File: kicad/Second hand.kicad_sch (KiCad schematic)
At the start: 66 parts, among them U001 74HC595, U002 74HC595

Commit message: First completely routed version
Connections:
- net Px0 renamed Sx0
- net Px1 renamed Sx1
- net Px2 renamed Sx2
- net Px3 renamed Sx3
- net Px4 renamed Sx4
- net Px5 renamed Sx5
- net Px6 renamed Sx6
- net Px7 renamed Sx7
- net Px8 renamed Sx8
- net Px9 renamed Sx9
- net Q0x renamed S0x
- net Q1x renamed S1x
- net Q2x renamed S2x
- net Q3x renamed S3x
- net Q4x renamed S4x
- net Q5x renamed S5x

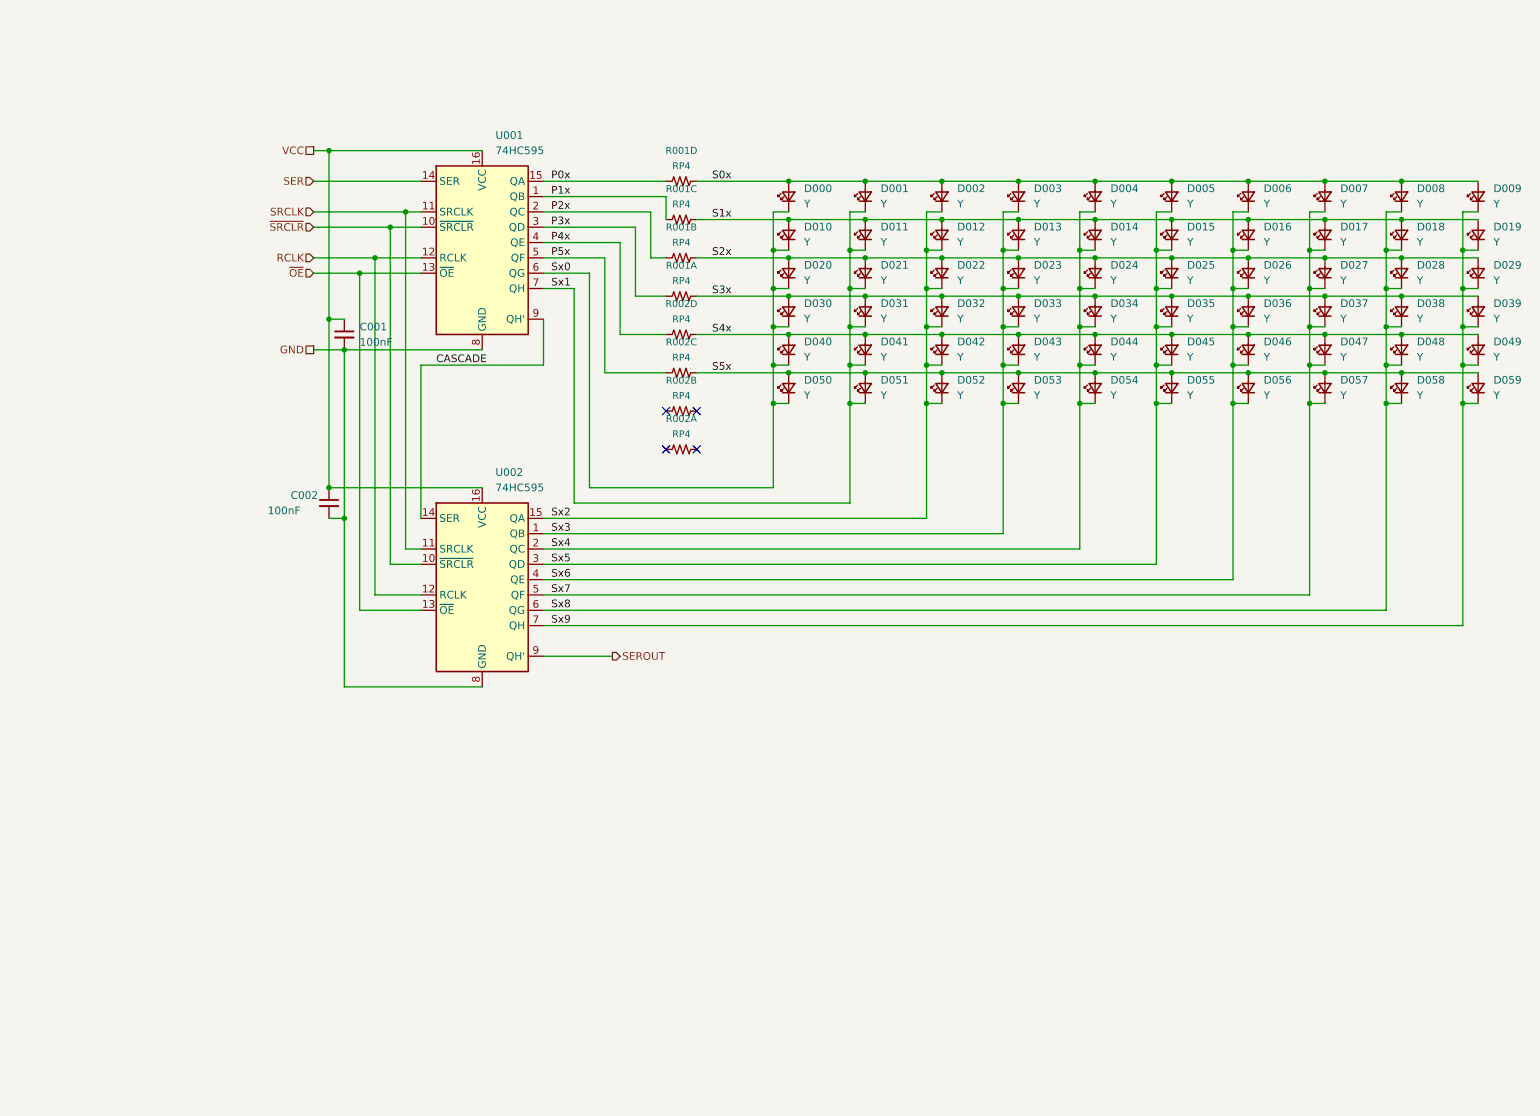
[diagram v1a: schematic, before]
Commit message: Add notes for diode voltages
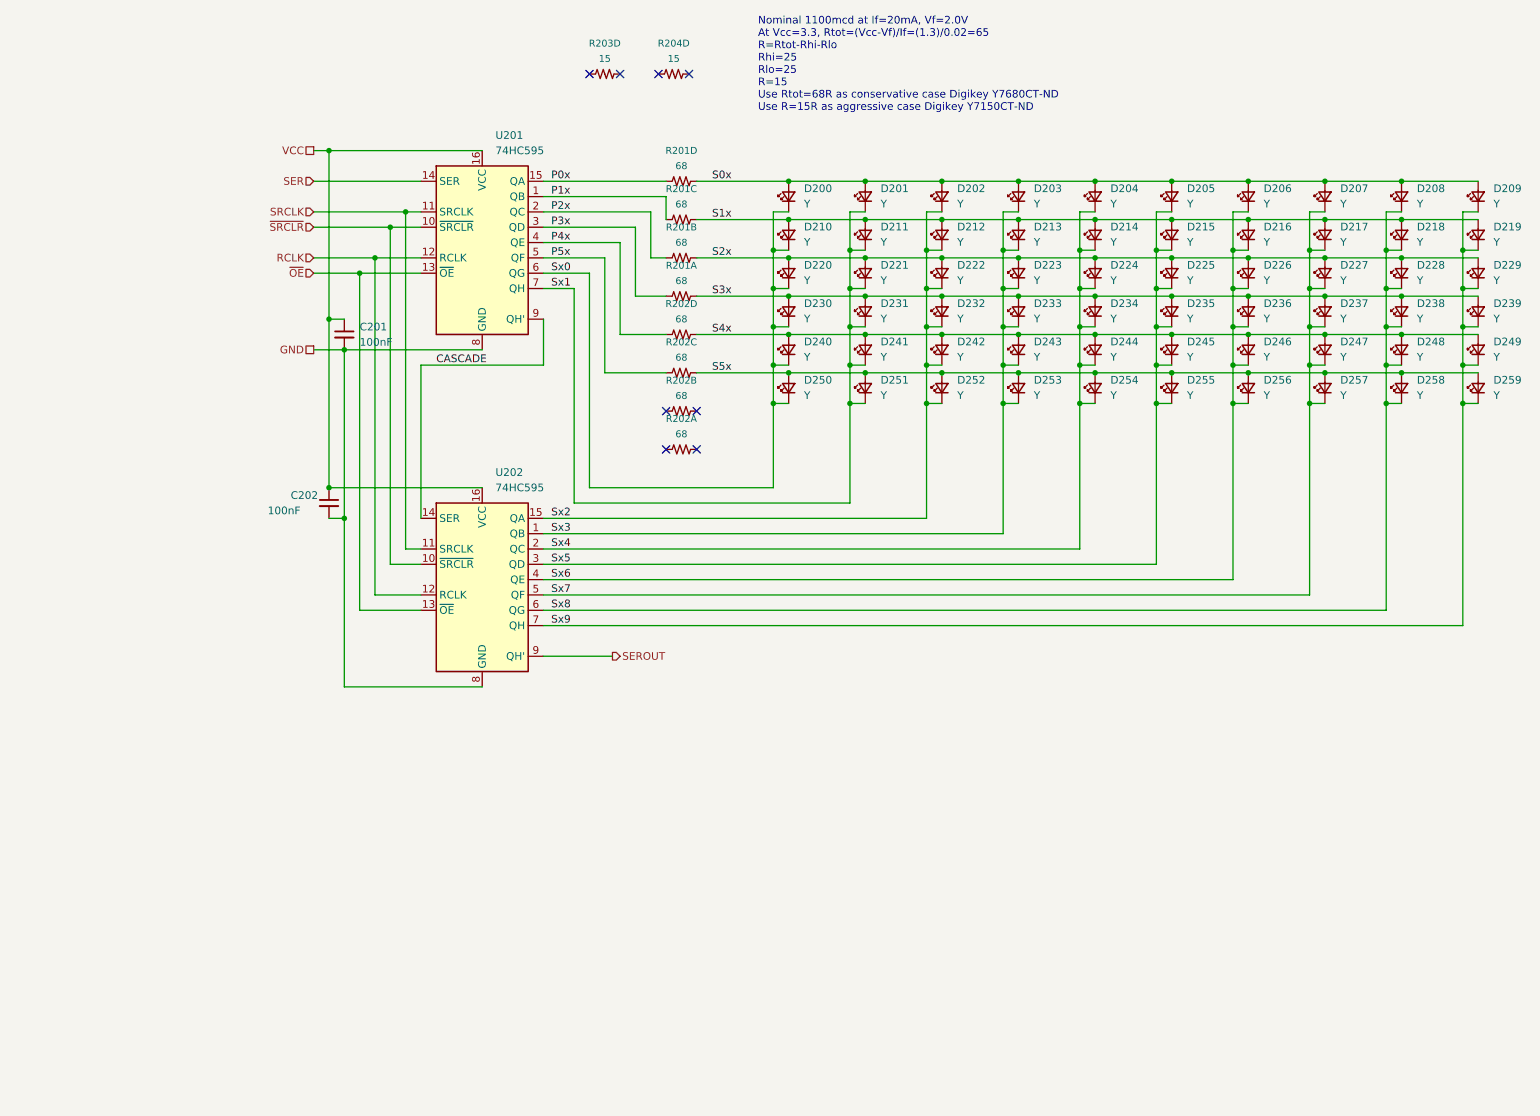
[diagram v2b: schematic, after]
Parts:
- added R203, R204: 15, KwanSystems:R_Array_Convex_4x0402, symbol KwanSystems:RP4
- C201: renamed from C001; Digikey (none) -> 445-5613-1-ND; Part Number (none) -> CGA2B1X7R1C104K050BC; Purpose (none) -> Second hand decoder bypass
- C202: renamed from C002; Digikey (none) -> 445-5613-1-ND; Part Number (none) -> CGA2B1X7R1C104K050BC; Purpose (none) -> Second hand decoder bypass
- D200: renamed from D000; Purpose (none) -> Yellow second hand
- D201: renamed from D001; Purpose (none) -> Yellow second hand
- D202: renamed from D002; Purpose (none) -> Yellow second hand
- D203: renamed from D003; Purpose (none) -> Yellow second hand
- D204: renamed from D004; Purpose (none) -> Yellow second hand
- D205: renamed from D005; Purpose (none) -> Yellow second hand
- D206: renamed from D006; Purpose (none) -> Yellow second hand
- D207: renamed from D007; Purpose (none) -> Yellow second hand
- D208: renamed from D008; Purpose (none) -> Yellow second hand
- D209: renamed from D009; Purpose (none) -> Yellow second hand
- D210: renamed from D010; Purpose (none) -> Yellow second hand
- D211: renamed from D011; Purpose (none) -> Yellow second hand
- D212: renamed from D012; Purpose (none) -> Yellow second hand
- D213: renamed from D013; Purpose (none) -> Yellow second hand
- D214: renamed from D014; Purpose (none) -> Yellow second hand
- D215: renamed from D015; Purpose (none) -> Yellow second hand
- D216: renamed from D016; Purpose (none) -> Yellow second hand
- D217: renamed from D017; Purpose (none) -> Yellow second hand
- D218: renamed from D018; Purpose (none) -> Yellow second hand
- D219: renamed from D019; Purpose (none) -> Yellow second hand
- D220: renamed from D020; Purpose (none) -> Yellow second hand
- D221: renamed from D021; Purpose (none) -> Yellow second hand
- D222: renamed from D022; Purpose (none) -> Yellow second hand
- D223: renamed from D023; Purpose (none) -> Yellow second hand
- D224: renamed from D024; Purpose (none) -> Yellow second hand
- D225: renamed from D025; Purpose (none) -> Yellow second hand
- D226: renamed from D026; Purpose (none) -> Yellow second hand
- D227: renamed from D027; Purpose (none) -> Yellow second hand
- D228: renamed from D028; Purpose (none) -> Yellow second hand
- D229: renamed from D029; Purpose (none) -> Yellow second hand
- D230: renamed from D030; Purpose (none) -> Yellow second hand
- D231: renamed from D031; Purpose (none) -> Yellow second hand
- D232: renamed from D032; Purpose (none) -> Yellow second hand
- D233: renamed from D033; Purpose (none) -> Yellow second hand
- D234: renamed from D034; Purpose (none) -> Yellow second hand
- D235: renamed from D035; Purpose (none) -> Yellow second hand
- D236: renamed from D036; Purpose (none) -> Yellow second hand
- D237: renamed from D037; Purpose (none) -> Yellow second hand
- D238: renamed from D038; Purpose (none) -> Yellow second hand
- D239: renamed from D039; Purpose (none) -> Yellow second hand
- D240: renamed from D040; Purpose (none) -> Yellow second hand
- D241: renamed from D041; Purpose (none) -> Yellow second hand
- D242: renamed from D042; Purpose (none) -> Yellow second hand
- D243: renamed from D043; Purpose (none) -> Yellow second hand
- D244: renamed from D044; Purpose (none) -> Yellow second hand
- D245: renamed from D045; Purpose (none) -> Yellow second hand
- D246: renamed from D046; Purpose (none) -> Yellow second hand
- D247: renamed from D047; Purpose (none) -> Yellow second hand
- D248: renamed from D048; Purpose (none) -> Yellow second hand
- D249: renamed from D049; Purpose (none) -> Yellow second hand
- D250: renamed from D050; Purpose (none) -> Yellow second hand
- D251: renamed from D051; Purpose (none) -> Yellow second hand
- D252: renamed from D052; Purpose (none) -> Yellow second hand
- D253: renamed from D053; Purpose (none) -> Yellow second hand
- D254: renamed from D054; Purpose (none) -> Yellow second hand
- D255: renamed from D055; Purpose (none) -> Yellow second hand
- D256: renamed from D056; Purpose (none) -> Yellow second hand
- D257: renamed from D057; Purpose (none) -> Yellow second hand
- D258: renamed from D058; Purpose (none) -> Yellow second hand
- D259: renamed from D059; Purpose (none) -> Yellow second hand
- R201: renamed from R001; value RP4 -> 68; Digikey (none) -> Y7680CT-ND; Part Number (none) -> EXB-28V680JX; Purpose (none) -> Second hand conservative current limit
- R202: renamed from R002; value RP4 -> 68; Digikey (none) -> Y7680CT-ND; Part Number (none) -> EXB-28V680JX; Purpose (none) -> Second hand conservative current limit
- U201: renamed from U001; Part Number (none) -> 74HC595PW,118; Purpose (none) -> Hand Decoder
- U202: renamed from U002; Part Number (none) -> 74HC595PW,118; Purpose (none) -> Hand Decoder
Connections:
- no-connect marks 4 -> 8
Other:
- note added: "Nominal 1100mcd at If=20mA, Vf=2.0V At Vcc=3.3, Rtot=(Vcc-Vf)/If=(1.3)/0.02=65 R=Rtot-Rhi-Rlo Rhi=25 Rlo=25 R=15 Use Rtot=68R as conservative case Digikey Y7680CT-ND Use R=15R as aggressive case Digikey Y7150CT-ND"

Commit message: Put MOSFET switch transistors in place. We won't end up using these.
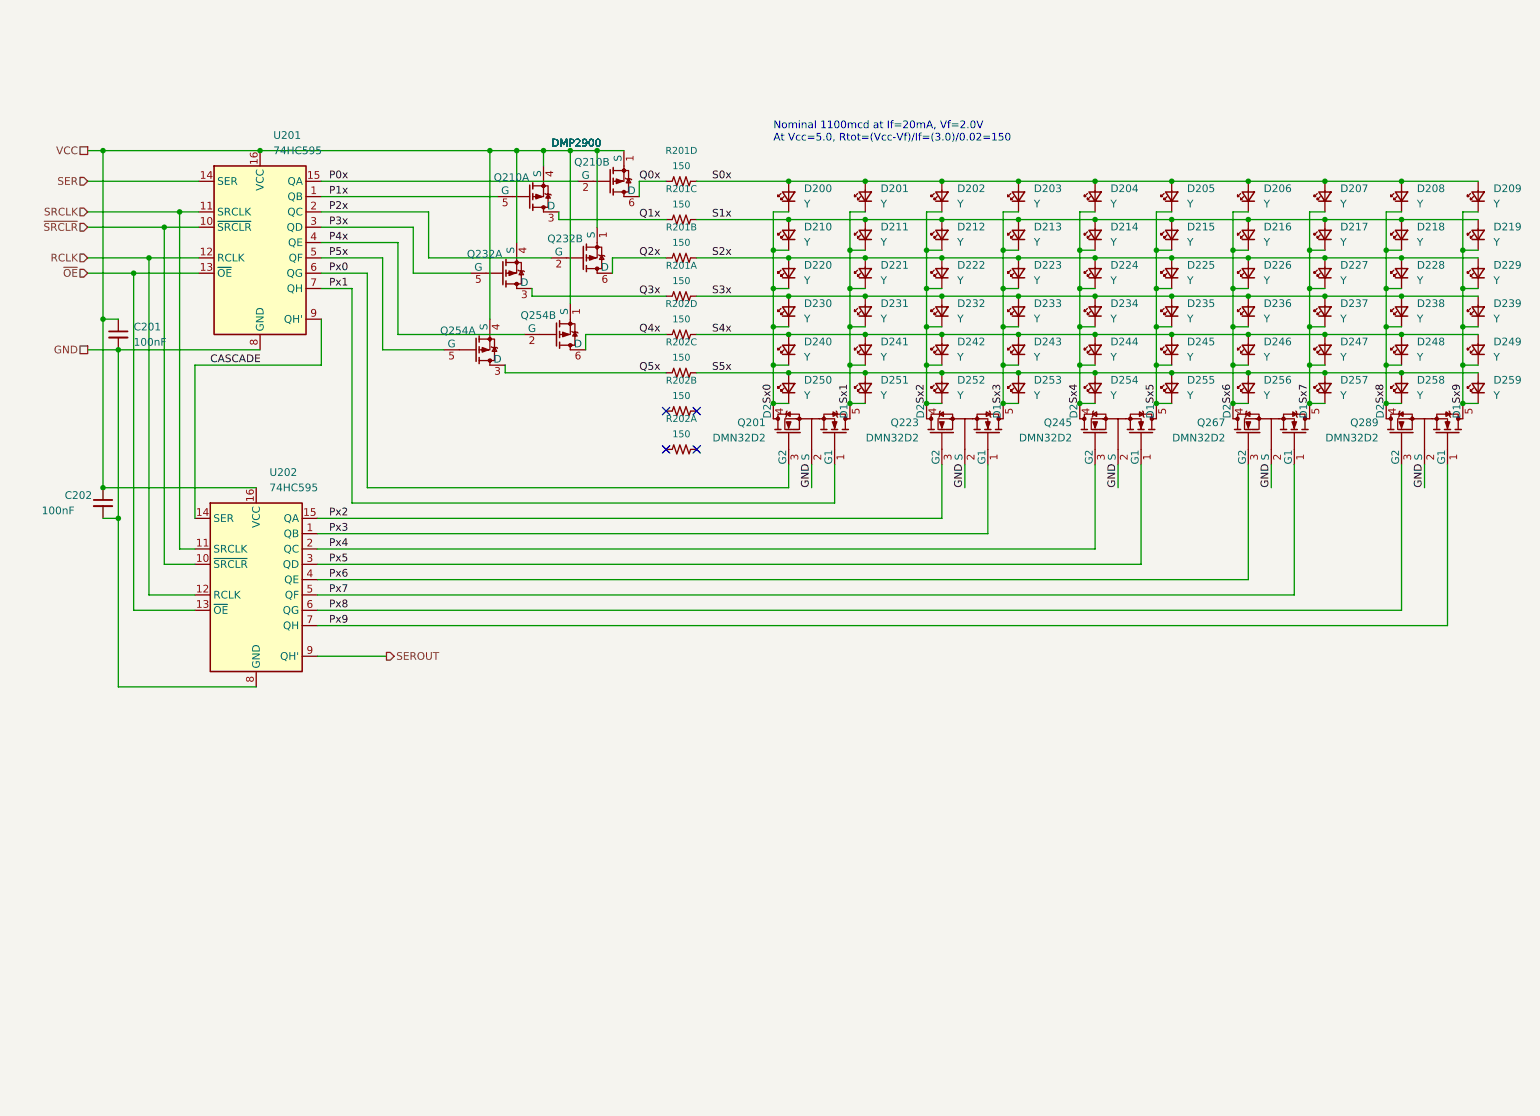
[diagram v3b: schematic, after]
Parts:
- removed R203, R204: 15, KwanSystems:R_Array_Convex_4x0402, symbol KwanSystems:RP4
- added Q201, Q223, Q245, Q267, Q289: DMN32D2, Package_TO_SOT_SMD:SOT-353_SC-70-5, symbol KwanSystems:NMOS_DUAL_COMMON_SOURCE
- added Q210, Q232, Q254: DMP2900, Package_TO_SOT_SMD:SOT-363_SC-70-6, symbol KwanSystems:PMOS_DUAL
- R201, R202: value 68 -> 150
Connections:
- net GND: now also Q201.2 (S), Q223.2 (S), Q245.2 (S), Q267.2 (S), Q289.2 (S)
- net P0x: now also Q210.2 (G); no longer R201.4
- net P1x: now also Q210.5 (G); no longer R201.3 (4)
- net P2x: now also Q232.2 (G); no longer R201.2 (4)
- net P3x: now also Q232.5 (G); no longer R201.1 (4)
- net P4x: now also Q254.2 (G); no longer R202.4
- net P5x: now also Q254.5 (G); no longer R202.3 (4)
- net Sx0: now also Q201.4 (D2); no longer U201.6 (QG)
- net Sx1: now also Q201.5 (D1); no longer U201.7 (QH)
- net Sx2: now also Q223.4 (D2); no longer U202.15 (QA)
- net Sx3: now also Q223.5 (D1); no longer U202.1 (QB)
- net Sx4: now also Q245.4 (D2); no longer U202.2 (QC)
- net Sx5: now also Q245.5 (D1); no longer U202.3 (QD)
- net Sx6: now also Q267.4 (D2); no longer U202.4 (QE)
- net Sx7: now also Q267.5 (D1); no longer U202.5 (QF)
- net Sx8: now also Q289.4 (D2); no longer U202.6 (QG)
- net Sx9: now also Q289.5 (D1); no longer U202.7 (QH)
- net VCC: now also Q210.1 (S), Q210.4 (S), Q232.1 (S), Q232.4 (S), Q254.1 (S), Q254.4 (S)
- new net Px0: Q201.3 (G2), U201.6 (QG)
- new net Px1: Q201.1 (G1), U201.7 (QH)
- new net Px2: Q223.3 (G2), U202.15 (QA)
- new net Px3: Q223.1 (G1), U202.1 (QB)
- new net Px4: Q245.3 (G2), U202.2 (QC)
- new net Px5: Q245.1 (G1), U202.3 (QD)
- new net Px6: Q267.3 (G2), U202.4 (QE)
- new net Px7: Q267.1 (G1), U202.5 (QF)
- new net Px8: Q289.3 (G2), U202.6 (QG)
- new net Px9: Q289.1 (G1), U202.7 (QH)
- new net Q0x: Q210.6 (D), R201.4
- new net Q1x: Q210.3 (D), R201.3 (4)
- new net Q2x: Q232.6 (D), R201.2 (4)
- new net Q3x: Q232.3 (D), R201.1 (4)
- new net Q4x: Q254.6 (D), R202.4
- new net Q5x: Q254.3 (D), R202.3 (4)
- no-connect marks 8 -> 4
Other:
- note added: "Nominal 1100mcd at If=20mA, Vf=2.0V At Vcc=5.0, Rtot=(Vcc-Vf)/If=(3.0)/0.02=150"
- note removed: "Nominal 1100mcd at If=20mA, Vf=2.0V At Vcc=3.3, Rtot=(Vcc-Vf)/If=(1.3)/0.02=65 R=Rtot-Rhi-Rlo Rhi=25 Rlo=25 R=15 Use Rtot=68R as conservative case Digikey Y7680CT-ND Use R=15R as aggressive case Digikey Y7150CT-ND"
- moved on the sheet: C201, C202, U201, U202
